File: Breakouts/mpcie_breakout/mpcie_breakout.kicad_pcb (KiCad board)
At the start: 2 copper layers, 73 x 42 mm, 28 parts, among them J1 9-39, J10 8-14,G, J2 1-9, J3 40-48,43-51, J4 PWR, J5 16-34, J6 USB, J7 SIM_Card, J8 USB_OTG, J9 APWR, U1 MPCIE-Socket

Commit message: Adding SIM net labels to mPCI-E breakout - SIM slot not fixed yet
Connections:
- net Net-(C9-Pad1) renamed /SIM_VCC
- net Net-(J10-Pad2) renamed /SIM_IO
- net Net-(J10-Pad3) renamed /SIM_CLK
- net Net-(J10-Pad4) renamed /SIM_RST
- net Net-(J7-Pad6) renamed /SIM_VPP
- J7 pad 8: GND -> (no net)
- U1 pad : GND -> (no net)
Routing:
- net GND: track 36.0 -> 18.1 mm, vias 16 -> 10
- net (no net): track 0.00 -> 17.9 mm, vias 0 -> 6

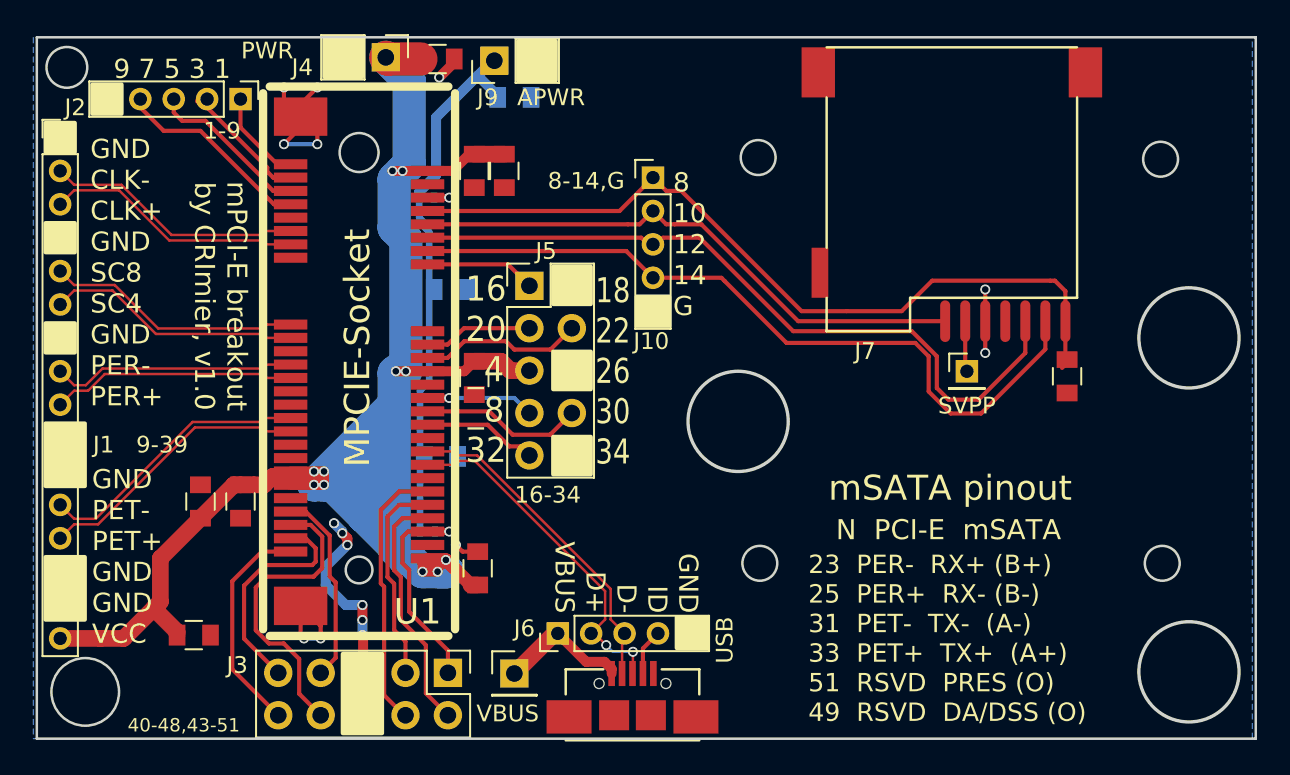
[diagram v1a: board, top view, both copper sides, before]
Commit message: Adding v2 of the mPCIe breakout with a README
Changelog in README
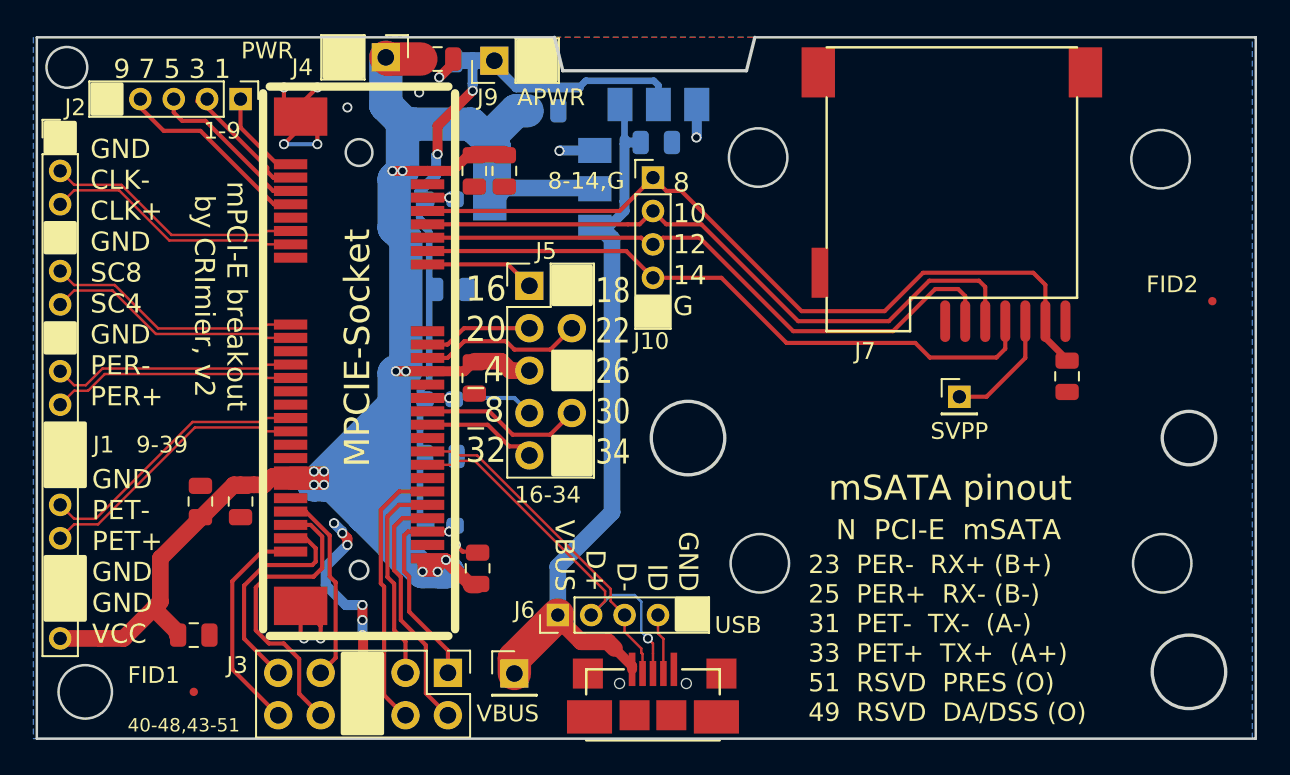
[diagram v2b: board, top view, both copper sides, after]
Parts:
- added C13: 100nF, Capacitor_SMD:C_0805_2012Metric, B.Cu at (191.3, 75.4)
- added C14: 100nF, Capacitor_SMD:C_0805_2012Metric, B.Cu at (198.1, 77.3)
- added FID1: Fiducial_0.5mm_Mask1.5mm, Fiducial:Fiducial_0.5mm_Mask1.5mm, F.Cu at (170.4, 110.2)
- added FID2: Fiducial_0.5mm_Mask1.5mm, Fiducial:Fiducial_0.5mm_Mask1.5mm, F.Cu at (231.4, 86.8)
- added U2: AP1117-33, Package_TO_SOT_SMD:SOT-223-3_TabPin2, B.Cu at (191.3, 80.1)
- added U3: AP1117-15, Package_TO_SOT_SMD:SOT-223-3_TabPin2, B.Cu at (198.2, 71.9)
- C1, C10, C11, C12, C2, C3, C4, C5, C6, C7, C8, C9: footprint Capacitors_SMD:C_0805 -> Capacitor_SMD:C_0805_2012Metric
- J8: footprint mpcie_breakout:MICROUSB_SIMPLE -> mpcie_breakout:MICROUSB_REINFORCED
- R1, R2, R3: footprint Resistors_SMD:R_0402 -> Resistor_SMD:R_0603_1608Metric_Pad1.05x0.95mm_HandSolder
- moved C10 5.03 mm to (185.1, 72.4), turned to 180 degrees
- moved TP1 1.59 mm to (216.2, 92.5)
- moved J8 1.22 mm to (197.9, 109.1)
- moved J6 1.10 mm to (192.2, 105.6)
- moved R3 0.85 mm to (185.2, 100.2)
- moved R1 0.83 mm to (185.2, 80.7)
- moved R2 0.73 mm to (185.1, 92.7)
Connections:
- net Net-(J6-Pad1) renamed VBUS
- J7 pad 8: (no net) -> GND
- U1 pad : (no net) -> GND
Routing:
- net VBUS: track 7.97 -> 49.8 mm
- net VCC: track 116.6 -> 135.8 mm
- net GND: track 18.1 -> 36.3 mm, vias 10 -> 18
- net (no net): track 17.9 -> 0.00 mm, vias 6 -> 0
- net +1V5: track 35.7 -> 47.8 mm, vias 0 -> 2
- net /SIM_CLK: track 44.3 -> 37.6 mm
- net /SIM_RST: track 45.5 -> 39.1 mm
- net /SIM_IO: track 34.1 -> 39.7 mm
- net /SIM_VPP: track 3.04 -> 7.11 mm
- net /D+: track 21.1 -> 24.0 mm, vias 2 -> 1
- net /D-: track 19.9 -> 20.9 mm
- net Net-(J3-Pad1): track 13.0 -> 12.1 mm
- net Net-(R1-Pad1): track 2.20 -> 1.30 mm
- net Net-(J6-Pad4): track 2.77 -> 3.63 mm
- net Net-(J5-Pad7): track 7.32 -> 6.47 mm
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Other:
- outline, holes or cut-outs redrawn
- board text added: "Using this in a project? Msg me on Tindie and tell me about it =)"
- board text added: "mPCI-E breakout by CRImier, v2"
- board text removed: "Using this in a project? Msg arsenijs@zerophone.org and tell me about it =)"
- board text removed: "mPCI-E breakout by CRImier, v1.0"

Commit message: Adding an ADJ resistor to the 1117-15 on the backside, rerouting diffpairs to decrease impedance a little bit
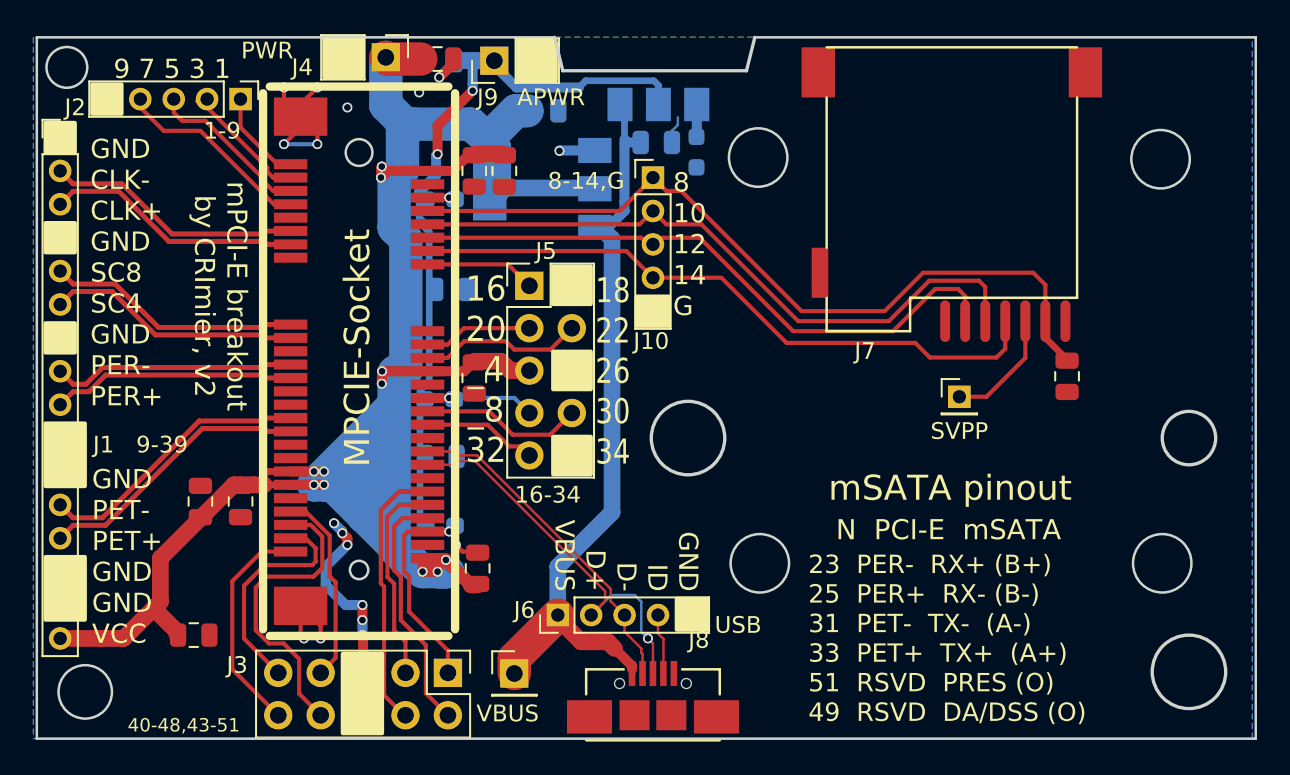
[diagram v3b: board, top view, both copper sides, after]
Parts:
- removed FID1, FID2: Fiducial_0.5mm_Mask1.5mm, Fiducial:Fiducial_0.5mm_Mask1.5mm
- added R4: 0/ADJ, Resistor_SMD:R_0603_1608Metric_Pad0.98x0.95mm_HandSolder, B.Cu at (200.5, 77.9)
- J8: footprint mpcie_breakout:MICROUSB_REINFORCED -> mpcie_breakout:MICROUSB_SIMPLE
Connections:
- U3 pad 1: GND -> Net-(R4-Pad1)
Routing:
- net Net-(R4-Pad1): track 0.00 -> 1.99 mm
- net VCC: track 135.8 -> 137.8 mm
- net GND: track 36.3 -> 36.0 mm, vias 18 -> 17

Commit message: mpcie_breakout: v3 files + panel files
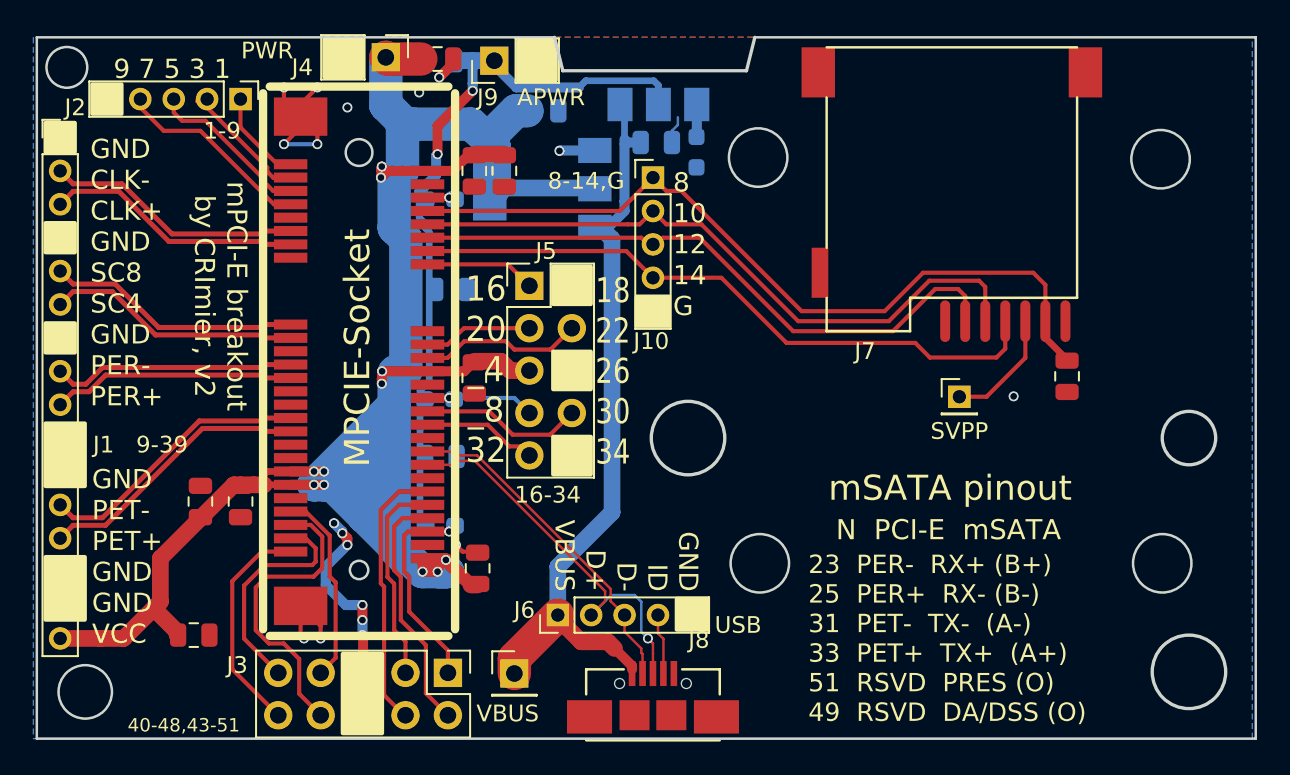
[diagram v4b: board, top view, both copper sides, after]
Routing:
- net GND: vias 17 -> 18
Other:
- net class Default removed
- board text added: "2 +3.3V 4 GND 6 +1.5V 8 S_VCC 10 S_IO 12 S_CLK 14 S_RST 16 S_VPP 18 GND 20 ~{W_DIS 22} PERST 24 +3.3V 26 GND 28 +1.5V 30 SMB_CK 32 SMB_IO 34 GND 36 D- 38 D+ 40 GND 42 ~{LED_WW 44} ~{LED_WL 46} ~{LED_WP 48} +1.5V 50 GND 52 +3.3V"
- board text added: "~{WAKE} 1 COEX1 3 COEX2 5 ~{CKREQ} 7 GND 9 CLK- 11 CLK+ 13 GND 15 S_C8 17 S_C4 19 GND 21 PER- 23 PER+ 25 GND 27 GND 29 PET- 31 PET+ 33 GND 35 GND 37 +3.3V 39 +3.3V 41 GND 43 RSVD 45 RSVD 47 RSVD 49 RSVD 51"
- board text removed: "2 +3.3V 4 GND 6 +1.5V 8 S_VCC 10 S_IO 12 S_CLK 14 S_RST 16 S_VPP 18 GND 20 ~W_DIS 22 PERST 24 +3.3V 26 GND 28 +1.5V 30 SMB_CK 32 SMB_IO 34 GND 36 D- 38 D+ 40 GND 42 ~LED_WW 44 ~LED_WL 46 ~LED_WP 48 +1.5V 50 GND 52 +3.3V"
- board text removed: "~WAKE~ 1 COEX1 3 COEX2 5 ~CKREQ~ 7 GND 9 CLK- 11 CLK+ 13 GND 15 S_C8 17 S_C4 19 GND 21 PER- 23 PER+ 25 GND 27 GND 29 PET- 31 PET+ 33 GND 35 GND 37 +3.3V 39 +3.3V 41 GND 43 RSVD 45 RSVD 47 RSVD 49 RSVD 51"
